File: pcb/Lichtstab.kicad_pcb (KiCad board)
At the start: 4 copper layers, 100.5 x 87.7 mm, 149 parts, among them CON1 MIKROBUS_HOST_CONN, CON2 MIKROBUS_MODULECONN, J1 RJ45_LED_Shielded, Q1 AO3407A, SW1 TS-1187A-B-A-B, SW2 TS-1187A-B-A-B, U1 ESP32-WROOM-32UE-N4, U10 HL2304, U11 LIS2DH12, U12 LIS2MDLTR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

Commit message: fix holes
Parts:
- moved R32 1.20 mm to (165.0, 56.1), turned to 0 degrees
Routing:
- net +12V: track 195.4 -> 190.2 mm
- net Net-(D7-K): track 4.09 -> 5.41 mm
- net GND: vias 102 -> 101
- net +3.3V: vias 82 -> 81

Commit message: review version
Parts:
- added C45: 330u / 25V, Capacitor_SMD:CP_Elec_8x10.5, F.Cu at (106.2, 65.0)
- added C46: 47uF, Capacitor_SMD:C_1206_3216Metric, F.Cu at (119.8, 67.0)
- added G***: LOGO, TheBrutzlers_Lib:approved_theBrutzler, F.Cu at (126.8, 113.0)
- added L5: 3.3µH / 3.1A, Inductor_SMD:L_Changjiang_FNR5030S, F.Cu at (115.2, 67.0)
- C1, C10, C12, C32, C36, C37, C38, C40, C9: footprint Capacitor_SMD:C_0805_2012Metric -> Capacitor_SMD:C_1206_3216Metric
- C4: value 1nF -> 1nF / 2KV
- C5, C6, C7, C8: value 10nF -> 10nF / 100V
- moved C12 11.5 mm to (102.5, 83.2)
- moved R1 5.58 mm to (109.2, 72.0), turned to -90 degrees
- moved U10 4.57 mm to (115.0, 62.3), turned to 90 degrees
- moved C3 2.00 mm to (107.5, 72.0)
- moved R2 2.00 mm to (101.6, 72.0)
- moved X1 2.00 mm to (104.5, 72.0)
- moved R22 1.25 mm to (132.0, 93.8)
- moved R23 1.00 mm to (130.2, 93.8)
- moved C32 0.75 mm to (92.2, 95.5)
- moved C38 0.75 mm to (128.2, 95.0)
- moved C1 0.51 mm to (117.8, 91.0)
- moved D10 0.50 mm to (114.0, 94.0)
- moved C10 0.50 mm to (110.5, 89.5)
- moved C28 0.50 mm to (116.3, 97.5)
- moved C30 0.50 mm to (111.3, 97.6)
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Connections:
- U2 pad 6: +12V_POE -> Net-(U2-+12V)
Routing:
- net +12V_POE: track 44.3 -> 83.5 mm, vias 8 -> 4
- net GND: track 102.9 -> 120.0 mm, vias 101 -> 105
- net Net-(U2-+12V): track 0.00 -> 13.2 mm
- net +12V?: track 210.4 -> 205.1 mm
- net Net-(D6-K): track 23.8 -> 27.7 mm
- net +3.3V: track 45.0 -> 48.6 mm, vias 81 -> 82
- net Net-(U10-G): track 4.12 -> 7.76 mm
- net /General/REF_CLK: track 82.9 -> 79.9 mm
- net Net-(D10-K): track 17.9 -> 16.5 mm
- net Net-(U3-LED0/PHYAD[0]/PMEB): track 44.0 -> 43.0 mm
- net Net-(U3-LED1/PHYAD[1]): track 58.8 -> 58.0 mm
- net Net-(U2-VB2): track 26.0 -> 26.8 mm
- net /General/ESP_IO39: track 142.1 -> 142.6 mm
- net /POE/TXCT: track 49.6 -> 50.1 mm
- removed copper zone on B.Cu, net +12V_POE
- removed copper zone on F.Cu, net +12V_POE

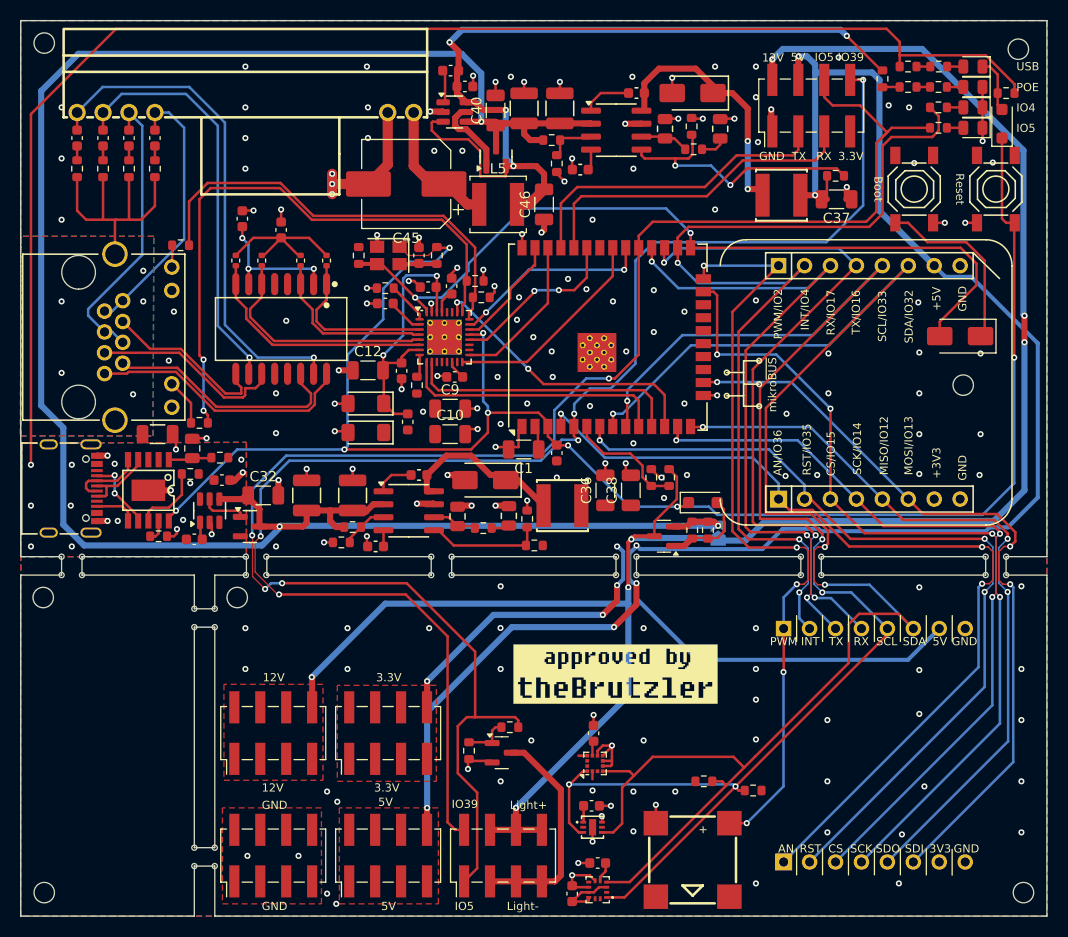
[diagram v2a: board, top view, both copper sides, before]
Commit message: remove third pcb and more flash
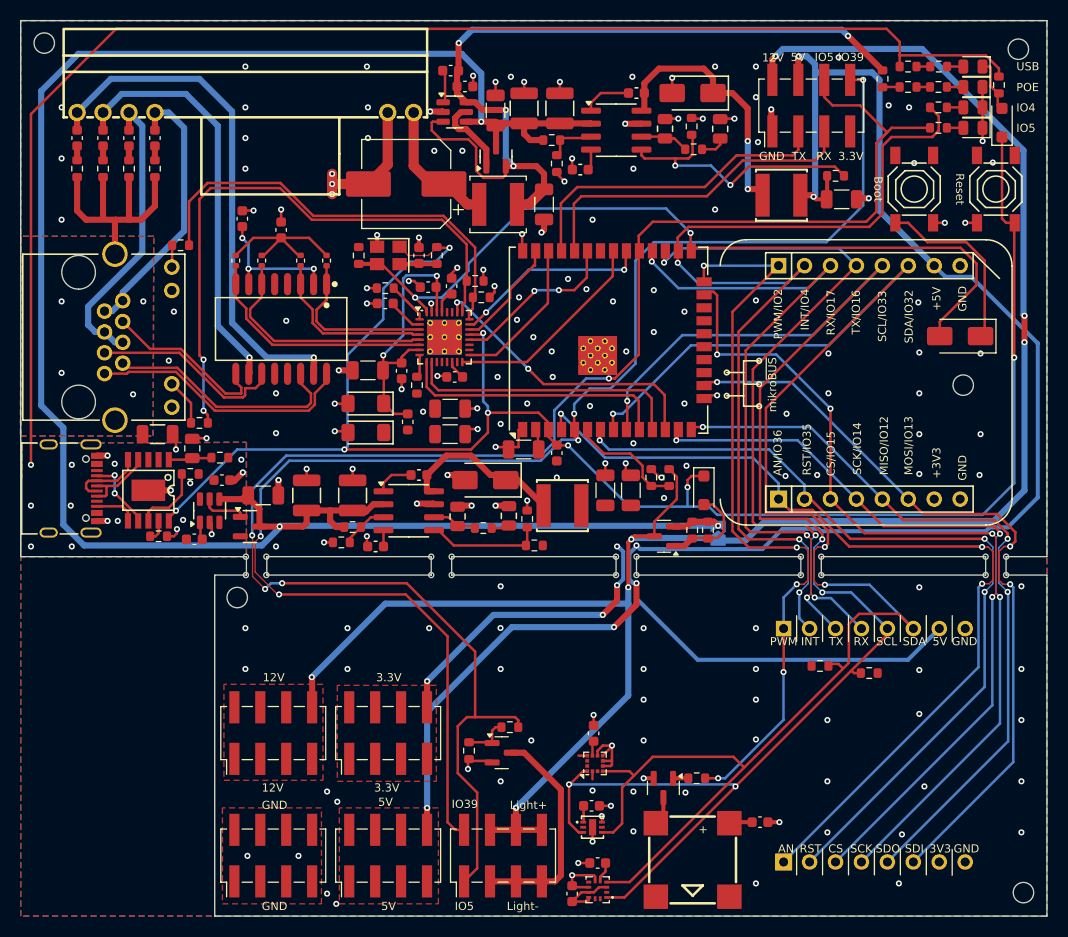
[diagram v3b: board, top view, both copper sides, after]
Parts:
- removed the REF** at (70.7, 105.5)
- removed the REF** at (86.5, 107.5)
- removed the REF** at (73.5, 102.4)
- removed the REF** at (70.8, 134.4)
- removed the REF** at (86.5, 130.9)
- added C47: 100nF, Capacitor_SMD:C_0603_1608Metric, F.Cu at (140.9, 127.5)
- added R46: 4.7kΩ, Resistor_SMD:R_0603_1608Metric, F.Cu at (134.7, 123.2)
- added U13: HL2304, Package_TO_SOT_SMD:SOT-23, F.Cu at (131.4, 124.2)
- G***: moved to B.Cu
- R14: value 2.49kΩ -> 2.49Ω
- R16, R17: value 10kΩ -> 2.49Ω
- U1: value ESP32-WROOM-32UE-N4 -> ESP32-WROOM-32UE-N8
- moved G*** 33.1 mm to (98.9, 130.8), turned to 180 degrees
- moved R41 16.2 mm to (151.6, 112.9)
- moved R40 16.0 mm to (146.8, 112.2)
- moved D9 1.20 mm to (135.4, 95.0), turned to -90 degrees
- moved R32 1.06 mm to (164.3, 55.3), turned to 90 degrees
- moved C37 0.50 mm to (148.9, 66.5)
- moved U1 0.31 mm to (126.1, 80.3)
- moved D8 0.10 mm to (164.6, 59.0)
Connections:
- net /General/EMAC_RXD+ renamed /General/EMAC_RXD0
- net /General/EMAC_RXD- renamed /General/EMAC_RXD1
- net /General/EMAC_TXD+ renamed /General/EMAC_TXD0
- net /General/EMAC_TXD- renamed /General/EMAC_TXD1
- BUZZER1 pad 1: /General/ESP_IO2 -> +3.3V
- BUZZER1 pad 2: GND -> Net-(U13-D)
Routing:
- net /General/ESP_IO2: track 76.0 -> 72.7 mm
- net /General/ESP_EN: track 172.4 -> 175.5 mm
- net Net-(U13-D): track 0.00 -> 2.82 mm
- net +3.3V: track 48.6 -> 50.9 mm
- net +12V_USB: track 139.1 -> 137.0 mm
- net Net-(U13-G): track 0.00 -> 1.49 mm
- net +12V_POE: track 83.5 -> 82.3 mm
- net /POE/TXCT: track 50.1 -> 51.3 mm
- net Net-(D9-A): track 8.62 -> 9.48 mm
- net GND: track 120.0 -> 120.5 mm, vias 105 -> 106
- net Net-(U2-VB1): track 28.8 -> 29.4 mm
- net Net-(C4-Pad2): vias 5 -> 4
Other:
- outline, holes or cut-outs redrawn
- board text removed: "JLCJLCJLCJLC"
